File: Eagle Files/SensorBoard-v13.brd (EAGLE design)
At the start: 76.5 x 33.5 mm, 48 parts, among them U2 METHANE_SENSOR

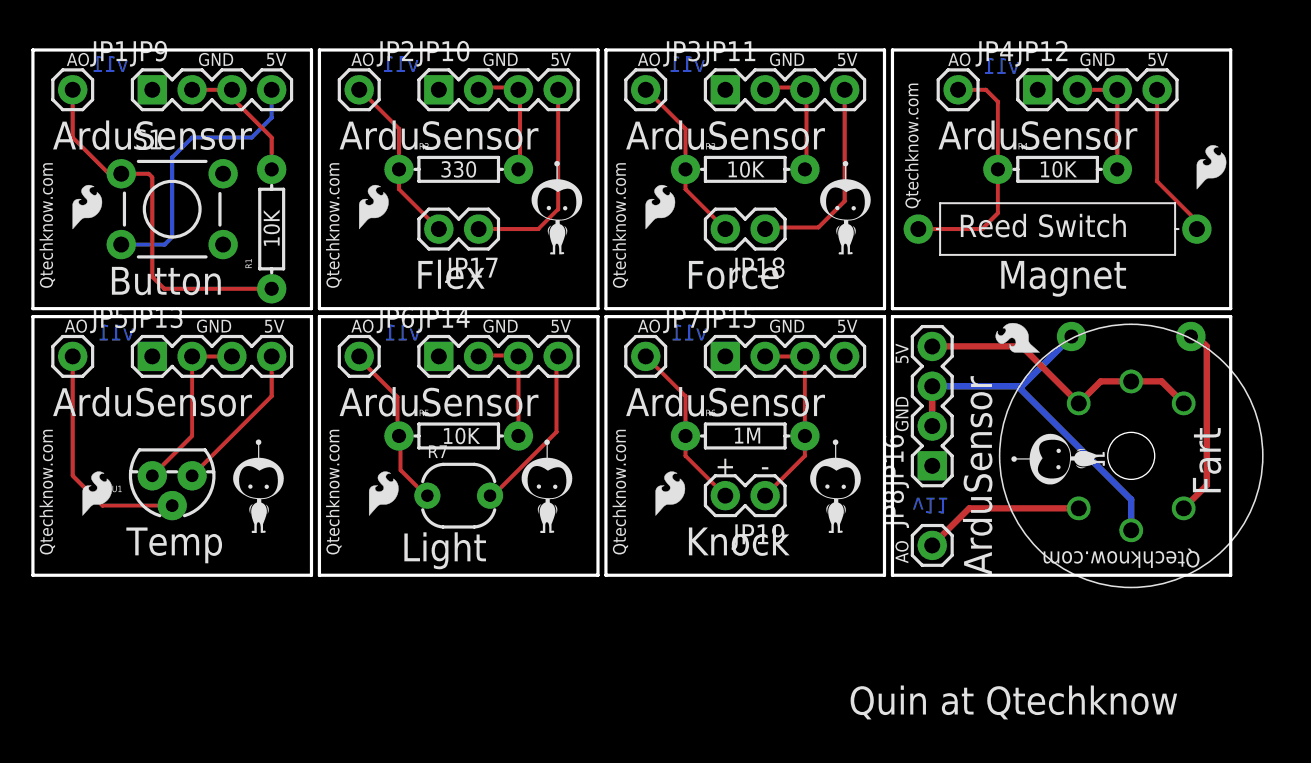
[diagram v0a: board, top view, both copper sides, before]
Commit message: fixed text and added OSHWA logo
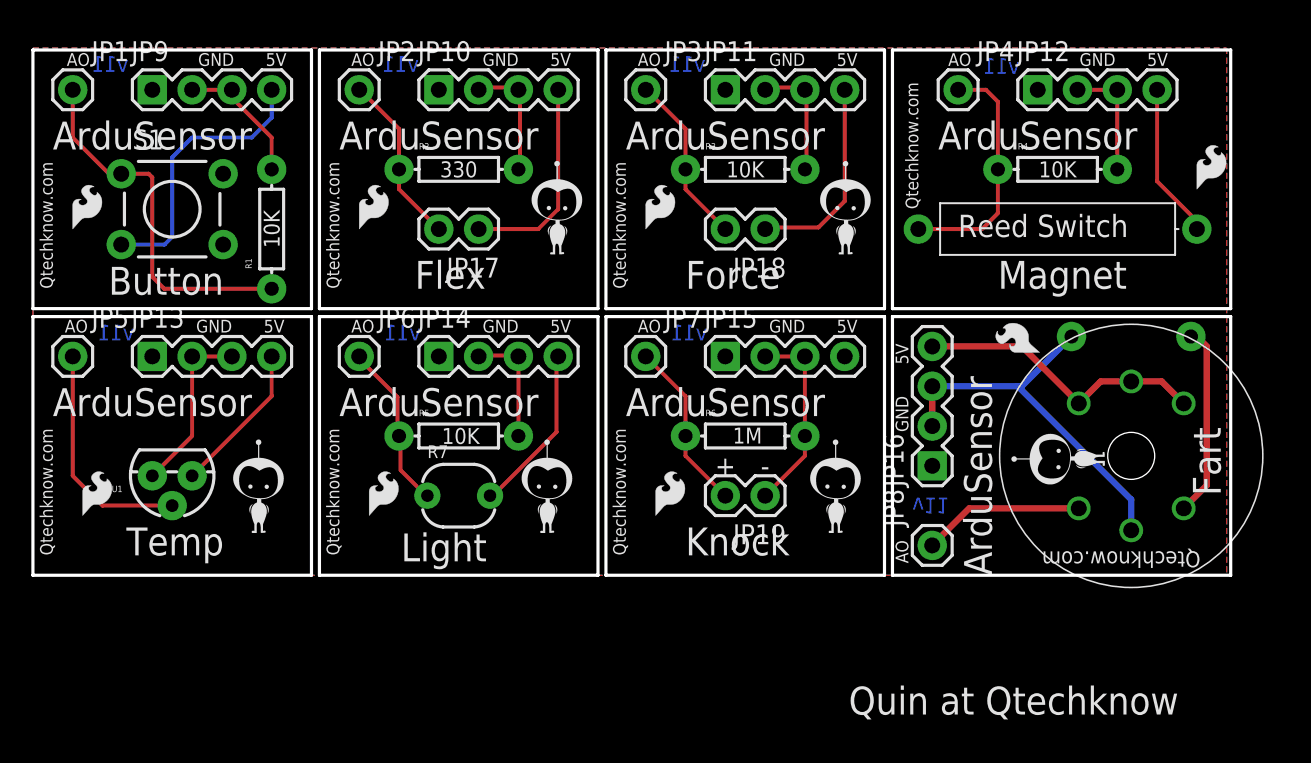
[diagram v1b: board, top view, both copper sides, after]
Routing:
- added copper zone on layer 1, net GND
- added copper zone on layer 16, net GND
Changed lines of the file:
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@@
 <text x="37.846" y="1.27" size="0.8128" layer="21" ratio="15" rot="R90">Qtechknow.com</text>
 <text x="53.169228125" y="0.800809375" size="1.4224" layer="22" ratio="15" rot="MR0">Qtechknow.com</text>
-<text x="44.196" y="6.985" size="1.27" layer="21" font="vector" ratio="16" align="center">+</text>
+<text x="44.196" y="6.985" size="1.27" layer="21" ratio="16" align="center">+</text>
 <text x="46.736" y="6.985" size="1.27" layer="21" ratio="16" align="center">-</text>
 <wire x1="36.068" y1="16.51" x2="36.068" y2="0" width="0.2032" layer="20"/>
@@
 <text x="57.785" y="27.178" size="1.778" layer="21" ratio="15">ArduSensor</text>
 <text x="59.055" y="21.59" size="1.4224" layer="21" ratio="15">Reed Switch</text>
-<text x="56.515" y="23.368" size="0.8128" layer="21" font="vector" ratio="16" rot="R90">Qtechknow.com</text>
+<text x="56.515" y="23.368" size="0.8128" layer="21" ratio="16" rot="R90">Qtechknow.com</text>
 <text x="75.3920625" y="17.761309375" size="1.778" layer="22" ratio="15" rot="MR0">Qtechknow.com</text>
 <text x="61.595" y="18.288" size="1.778" layer="21" ratio="15">Magnet</text>
@@
 <wire x1="36.576" y1="16.51" x2="54.356" y2="16.51" width="0.2032" layer="20"/>
 <wire x1="54.864" y1="16.51" x2="76.454" y2="16.51" width="0.2032" layer="20"/>
-<text x="6.096" y="32.131" size="1.016" layer="16" font="vector" ratio="15" rot="MR0">v11</text>
-<text x="24.638" y="32.131" size="1.016" layer="16" font="vector" ratio="15" rot="MR0">v11</text>
-<text x="42.926" y="32.131" size="1.016" layer="16" font="vector" ratio="15" rot="MR0">v11</text>
-<text x="62.992" y="32.004" size="1.016" layer="16" font="vector" ratio="15" rot="MR0">v11</text>
-<text x="56.134" y="4.953" size="1.016" layer="16" font="vector" ratio="15" rot="SMR180">v11</text>
-<text x="43.053" y="14.986" size="1.016" layer="16" font="vector" ratio="15" rot="MR0">v11</text>
-<text x="24.765" y="14.986" size="1.016" layer="16" font="vector" ratio="15" rot="MR0">v11</text>
-<text x="6.477" y="14.986" size="1.016" layer="16" font="vector" ratio="15" rot="MR0">v11</text>
+<text x="6.096" y="32.131" size="1.016" layer="16" ratio="15" rot="MR0">v11</text>
+<text x="24.638" y="32.131" size="1.016" layer="16" ratio="15" rot="MR0">v11</text>
+<text x="42.926" y="32.131" size="1.016" layer="16" ratio="15" rot="MR0">v11</text>
+<text x="62.992" y="32.004" size="1.016" layer="16" ratio="15" rot="MR0">v11</text>
+<text x="56.134" y="4.953" size="1.016" layer="16" ratio="15" rot="SMR180">v11</text>
+<text x="43.053" y="14.986" size="1.016" layer="16" ratio="15" rot="MR0">v11</text>
+<text x="24.765" y="14.986" size="1.016" layer="16" ratio="15" rot="MR0">v11</text>
+<text x="6.477" y="14.986" size="1.016" layer="16" ratio="15" rot="MR0">v11</text>
 <text x="58.42" y="32.512" size="0.8128" layer="21" font="vector" ratio="15">AO</text>
 <text x="66.802" y="32.512" size="0.8128" layer="21" font="vector" ratio="15">GND</text>
@@
 <text x="28.702" y="32.512" size="0.8128" layer="21" font="vector" ratio="15">GND</text>
 <text x="33.02" y="32.512" size="0.8128" layer="21" font="vector" ratio="15">5V</text>
-<text x="2.159" y="32.512" size="0.8128" layer="21" font="vector" ratio="15">AO</text>
-<text x="10.541" y="32.512" size="0.8128" layer="21" font="vector" ratio="15">GND</text>
-<text x="14.859" y="32.512" size="0.8128" layer="21" font="vector" ratio="15">5V</text>
+<text x="2.159" y="32.512" size="0.8128" layer="21" ratio="15">AO</text>
+<text x="10.541" y="32.512" size="0.8128" layer="21" ratio="15">GND</text>
+<text x="14.859" y="32.512" size="0.8128" layer="21" ratio="15">5V</text>
 <text x="2.032" y="15.494" size="0.8128" layer="21" font="vector" ratio="15">AO</text>
 <text x="10.414" y="15.494" size="0.8128" layer="21" font="vector" ratio="15">GND</text>
@@
 <text x="28.702" y="15.494" size="0.8128" layer="21" font="vector" ratio="15">GND</text>
 <text x="33.02" y="15.494" size="0.8128" layer="21" font="vector" ratio="15">5V</text>
-<text x="38.608" y="15.494" size="0.8128" layer="21" font="vector" ratio="15">AO</text>
-<text x="46.99" y="15.494" size="0.8128" layer="21" font="vector" ratio="15">GND</text>
-<text x="51.308" y="15.494" size="0.8128" layer="21" font="vector" ratio="15">5V</text>
-<text x="55.88" y="0.762" size="0.8128" layer="21" font="vector" ratio="15" rot="R90">AO</text>
-<text x="55.88" y="9.144" size="0.8128" layer="21" font="vector" ratio="15" rot="R90">GND</text>
-<text x="55.88" y="13.462" size="0.8128" layer="21" font="vector" ratio="15" rot="R90">5V</text>
+<text x="38.608" y="15.494" size="0.8128" layer="21" ratio="15">AO</text>
+<text x="46.99" y="15.494" size="0.8128" layer="21" ratio="15">GND</text>
+<text x="51.308" y="15.494" size="0.8128" layer="21" ratio="15">5V</text>
+<text x="55.88" y="0.762" size="0.8128" layer="21" ratio="15" rot="R90">AO</text>
+<text x="55.88" y="9.144" size="0.8128" layer="21" ratio="15" rot="R90">GND</text>
+<text x="55.88" y="13.462" size="0.8128" layer="21" ratio="15" rot="R90">5V</text>
 <text x="52.07" y="-8.89" size="1.778" layer="25" font="vector" ratio="15">Quin at Qtechknow</text>
 <text x="2.54" y="29.21" size="1.016" layer="22" ratio="15" rot="SMR270" align="center-left">A0</text>
@@
 <text x="59.055" y="9.525" size="1.016" layer="22" ratio="15" rot="SMR180" align="center-left">GND</text>
 <text x="59.055" y="12.065" size="1.016" layer="22" ratio="15" rot="SMR180" align="center-left">GND</text>
-<text x="27.305" y="8.89" size="1.016" layer="21" font="vector" ratio="16" align="center">10K</text>
-<text x="27.178" y="25.908" size="1.016" layer="21" font="vector" ratio="16" align="center">330</text>
-<text x="45.466" y="25.908" size="1.016" layer="21" font="vector" ratio="16" align="center">10K</text>
-<text x="65.405" y="25.908" size="1.016" layer="21" font="vector" ratio="16" align="center">10K</text>
-<text x="15.24" y="22.098" size="1.016" layer="21" font="vector" ratio="16" rot="R90" align="center">10K</text>
-<text x="70.104" y="15.24" size="1.016" layer="22" font="vector" ratio="16" rot="SMR0" align="center">10K</text>
-<text x="45.6057" y="8.9154" size="1.016" layer="21" font="vector" ratio="16" align="center">1M</text>
+<text x="27.305" y="8.89" size="1.016" layer="21" ratio="16" align="center">10K</text>
+<text x="27.178" y="25.908" size="1.016" layer="21" ratio="16" align="center">330</text>
+<text x="45.466" y="25.908" size="1.016" layer="21" ratio="16" align="center">10K</text>
+<text x="65.405" y="25.908" size="1.016" layer="21" ratio="16" align="center">10K</text>
+<text x="15.24" y="22.098" size="1.016" layer="21" ratio="16" rot="R90" align="center">10K</text>
+<text x="70.104" y="15.24" size="1.016" layer="22" ratio="16" rot="SMR0" align="center">10K</text>
+<text x="45.6057" y="8.9154" size="1.016" layer="21" ratio="16" align="center">1M</text>
 </plain>
 <attributes>
@@
 <wire x1="15.24" y1="13.97" x2="15.24" y2="11.43" width="0.254" layer="1"/>
 </signal>
+<signal name="GND">
+<polygon width="0.4064" layer="16" isolate="0.3048">
+<vertex x="0" y="33.655"/>
+<vertex x="76.2" y="33.655"/>
+<vertex x="76.2" y="0"/>
+<vertex x="0" y="0"/>
+</polygon>
+<polygon width="0.4064" layer="1" isolate="0.3048">
+<vertex x="0" y="33.655"/>
+<vertex x="76.2" y="33.655"/>
+<vertex x="76.2" y="0"/>
+<vertex x="0" y="0"/>
+</polygon>
+</signal>
 </signals>

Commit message: added better Qtechknow logo dude to the boards
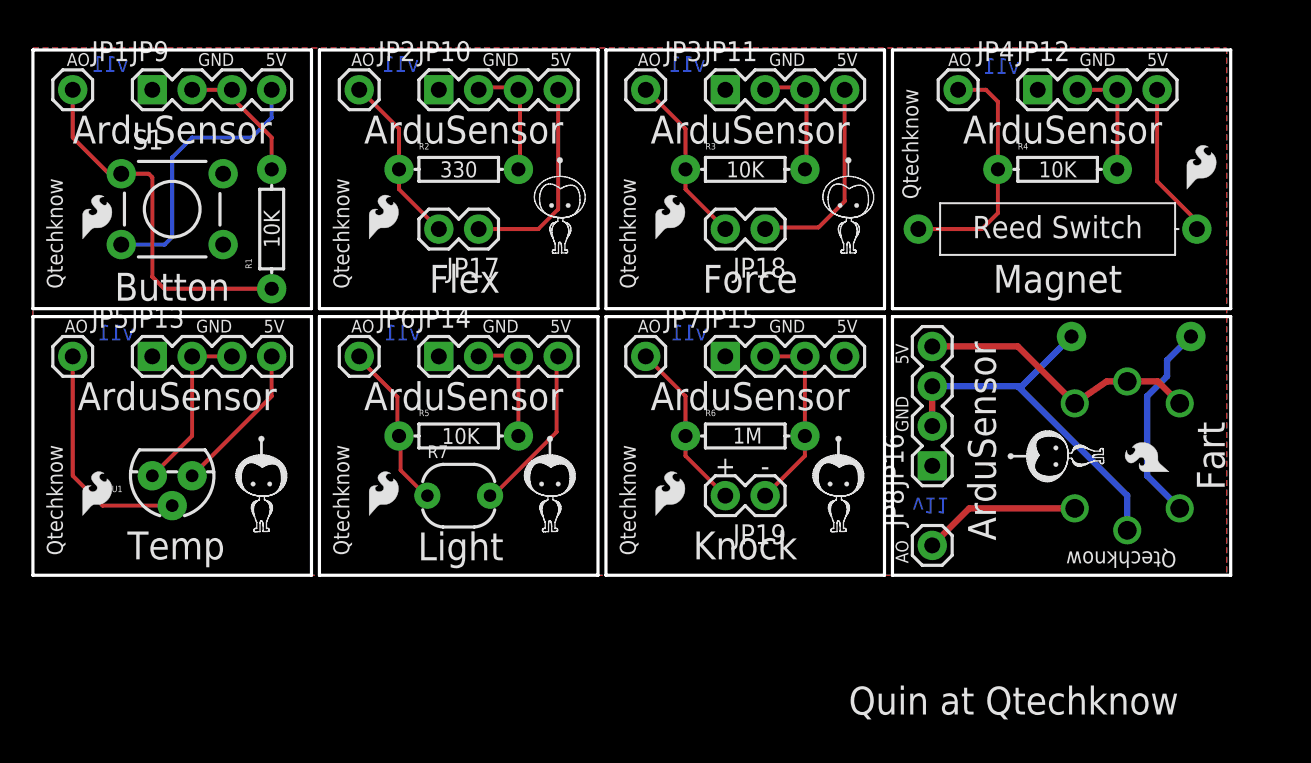
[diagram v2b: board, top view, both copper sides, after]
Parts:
- removed U$7, U$8: (no value), Qtechknow:QTK_GUYXS
- removed U2: METHANE_SENSOR, 1_SFE Sensors:MQ-3
- added U$21, U$22, U$23: MIGHTYQ-S-SILK, Qtechknow:LOGO-SMALL-SILK
- U$1: value (none) -> GAS-SENSORNEW; device Qtechknow:QTK_GUYXS -> Qtechknow:GAS_SENSOR
- U$2, U$3, U$4, U$6: device Qtechknow:QTK_GUYXS -> Qtechknow:LOGO-SMALL-FILL-SILK
- U$5: value (none) -> MIGHTYQ-S-SILK; device Qtechknow:QTK_GUYXS -> Qtechknow:LOGO-SMALL-SILK
- moved U$2 40.9 mm to (14.6, 5.08)
- moved U$1 39.9 mm to (69.8, 7.62), turned to 90 degrees
- moved U$3 37.5 mm to (33.0, 5.08), flipped to the top
- moved U$5 23.9 mm to (5.08, 27.3), flipped to the bottom
- moved U$4 19.1 mm to (51.4, 5.08)
- moved U$6 15.5 mm to (66.0, 7.62), turned to 90 degrees
- moved LOGO2 11.2 mm to (72.5, 6.60)
- moved LOGO6 0.90 mm to (21.5, 21.5)
- moved LOGO1 0.90 mm to (3.17, 21.5)
- moved LOGO5 0.90 mm to (39.8, 21.5)
- moved LOGO3 0.64 mm to (73.7, 24.6)
- renumbered 1_R1 to R8
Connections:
- net 1_N$1: now also U$1.1; no longer U2.A1
- net 1_N$2: now also U$1.4, U$1.5, U$1.6; no longer U2.B1, U2.B2, U2.HB
- net 1_N$3: now also U$1.2; no longer U2.HA
- net 1_N$4: now also U$1.3; no longer U2.A2
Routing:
- net 1_N$4: track 12.2 -> 13.0 mm
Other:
- board text added: "Qtechknow"
